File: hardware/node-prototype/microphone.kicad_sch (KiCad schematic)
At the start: 1 part, among them U2 MAX9814

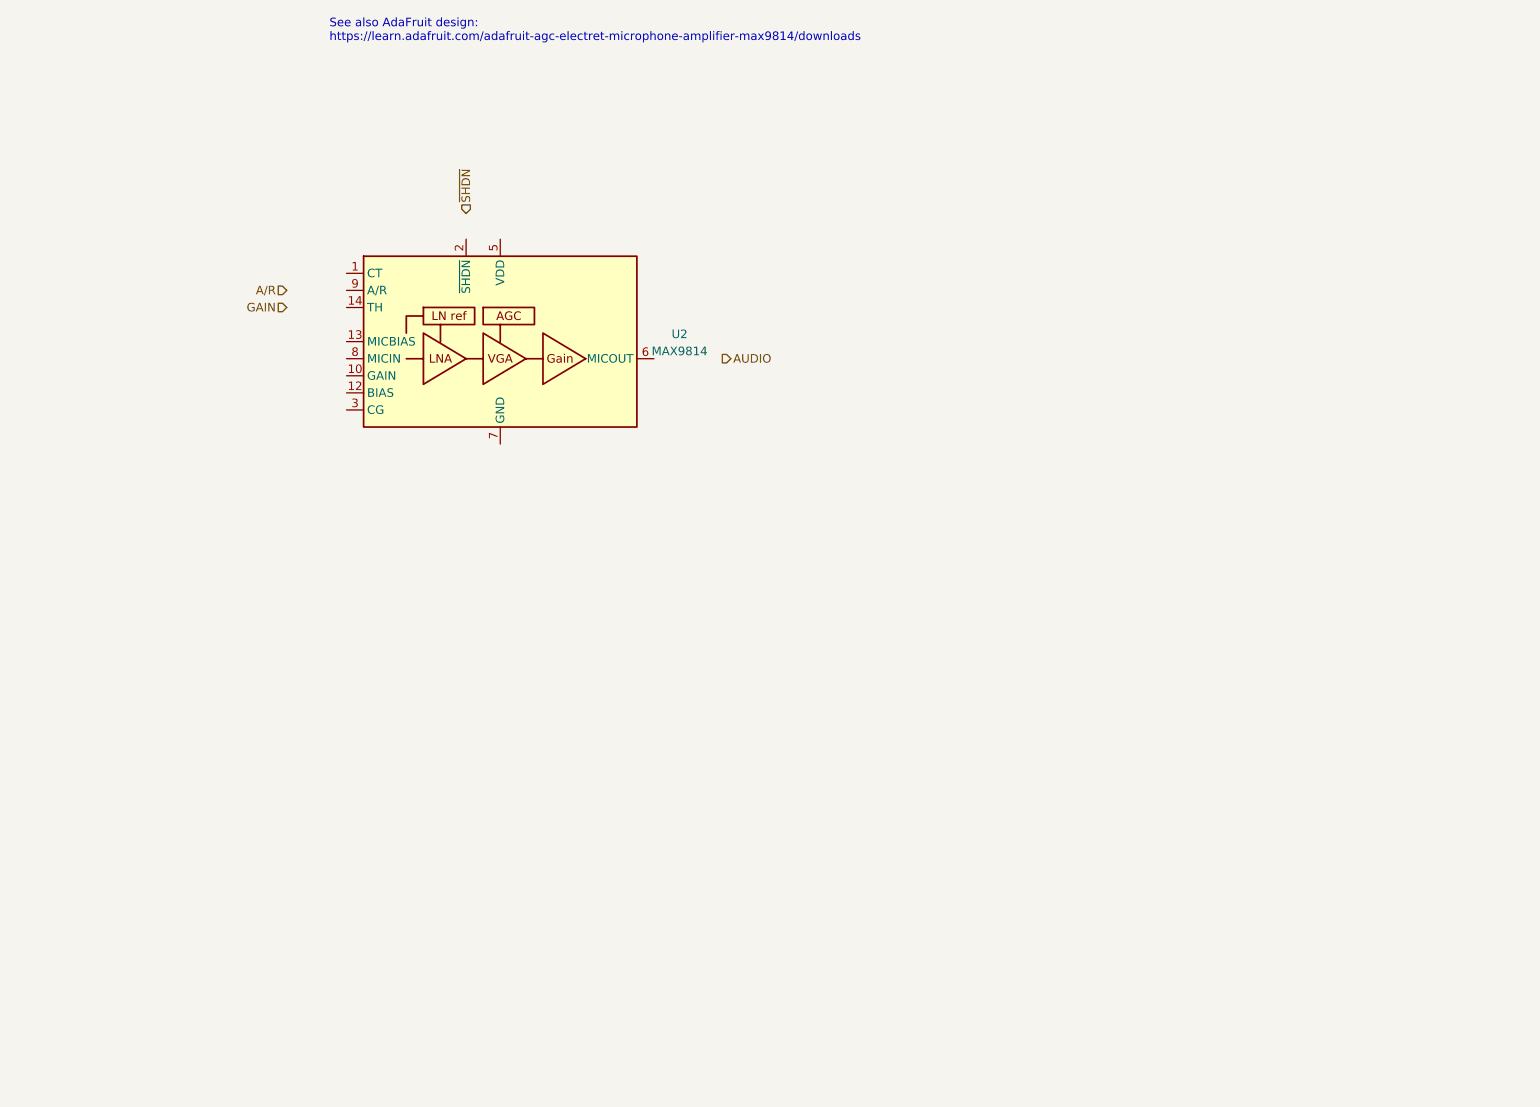
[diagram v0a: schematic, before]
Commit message: Design microphone component
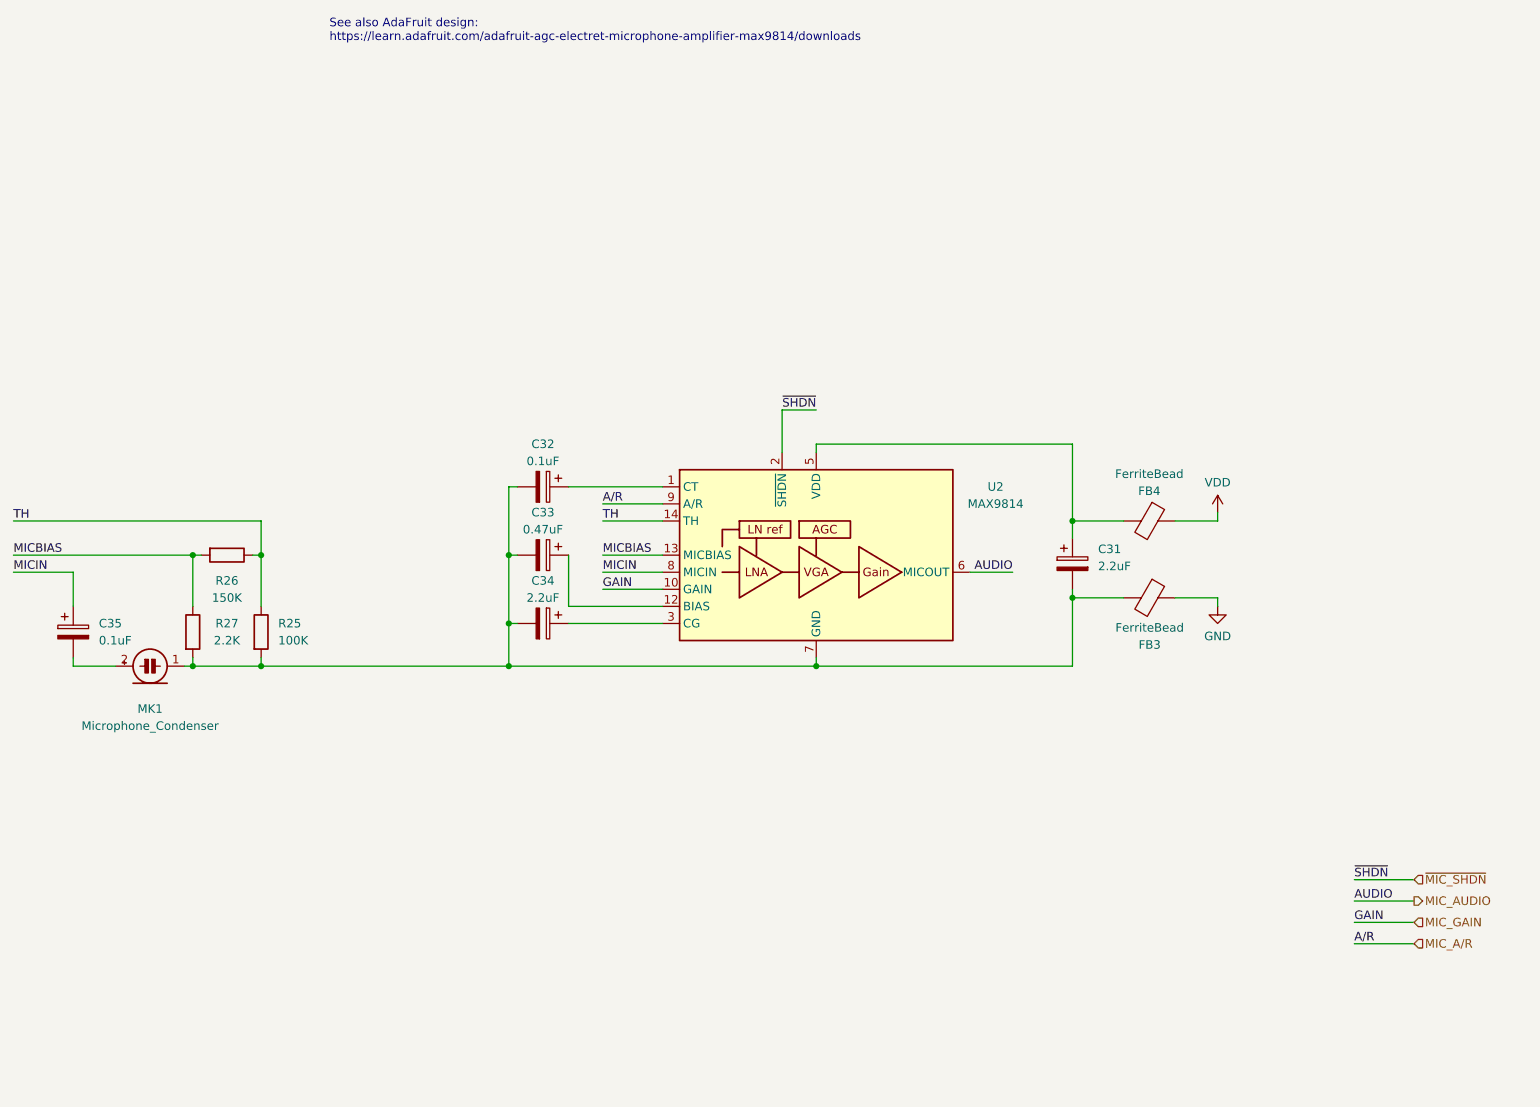
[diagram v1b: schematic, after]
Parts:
- added C31, C34: 2.2uF, symbol Device:C_Polarized
- added C32, C35: 0.1uF, symbol Device:C_Polarized
- added C33: 0.47uF, symbol Device:C_Polarized
- added FB3, FB4: FerriteBead, symbol Device:FerriteBead
- added MK1: Microphone_Condenser, symbol Device:Microphone_Condenser
- added R25: 100K, symbol Device:R
- added R26: 150K, symbol Device:R
- added R27: 2.2K, symbol Device:R
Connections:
- net at U2.1 (CT): now also C32.1
- net MIC_GAIN: now reaches U2.10 (GAIN)
- net at U2.11 (GND), U2.15 (GND), U2.4 (GND)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: now also C31.2, C32.2, C33.2, C34.2, FB3.2, MK1.1 (-), R25.2, R27.2
- net at U2.12 (BIAS): now also C33.1
- net MICBIAS: now reaches U2.13 (MICBIAS)
- net MICBIAS: now also R26.2, R27.1
- net TH: now reaches U2.14 (TH)
- net TH: now also R25.1, R26.1
- net ~{MIC_SHDN}: now reaches U2.2 (~{SHDN})
- net at U2.3 (CG): now also C34.1
- net at U2.5 (VDD): now also C31.1, FB4.2
- net MIC_AUDIO: now reaches U2.6 (MICOUT)
- net MICIN: now reaches U2.8 (MICIN)
- net MICIN: now also C35.1
- net MIC_A/R: now reaches U2.9 (A/R)
- new net: C35.2, MK1.2 (+)
- new net GND: FB3.1
- new net VDD: FB4.1
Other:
- moved on the sheet: U2

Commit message: WIP on user interface
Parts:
- removed FB3, FB4: FerriteBead, symbol Device:FerriteBead
- added R41: 10k, symbol Device:R
- R30: renamed from R27; value 2.2K -> 2.2k
- R31: renamed from R26; value 150K -> 150k
- R32: renamed from R25; value 100K -> 100k
- renumbered C35 to C31, C31 to C35, U2 to U10
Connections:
- net GND: now also C32.2, C33.2, C34.2, C35.2, MK1.1 (-), R30.2, R32.2, U10.11 (GND), U10.15 (GND), U10.4 (GND), U10.7 (GND), R41.2
- net ~{MIC_SHDN}: now also R41.1
- net VDDA: now reaches C35.1, U10.5 (VDD)

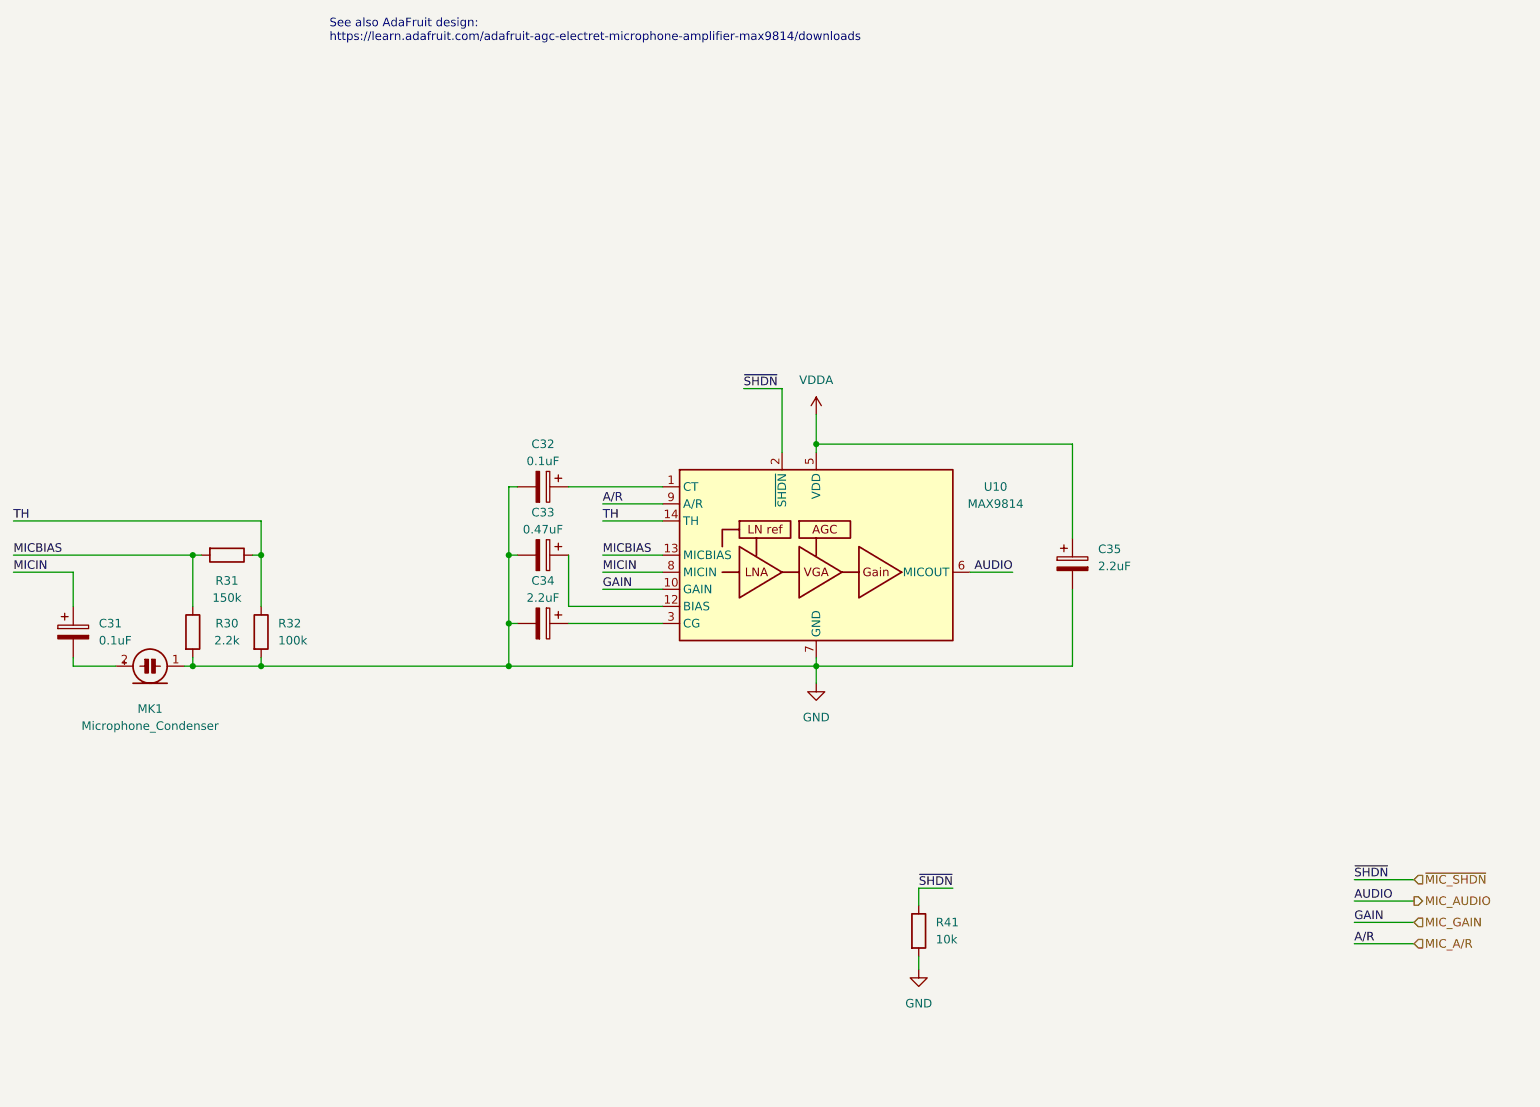
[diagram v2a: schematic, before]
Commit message: Plug schematic together
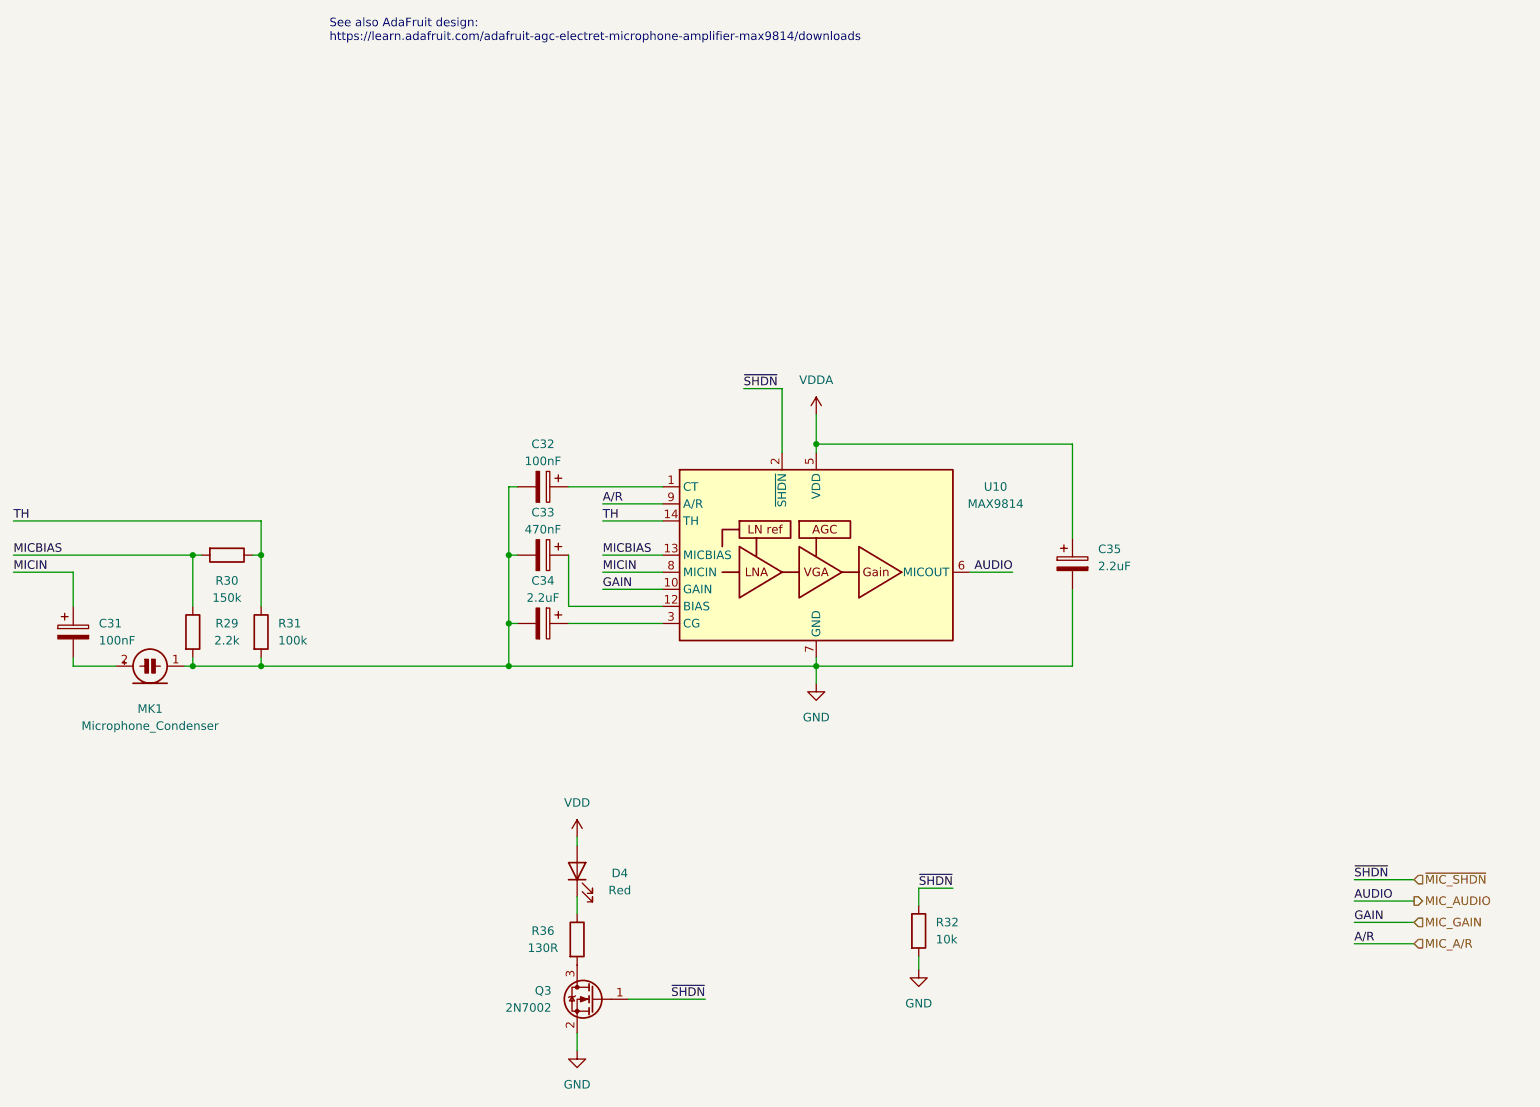
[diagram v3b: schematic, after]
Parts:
- added D4: Red, LED_SMD:LED_0603_1608Metric, symbol Device:LED
- added Q3: 2N7002, Package_TO_SOT_SMD:SOT-23, symbol Transistor_FET:2N7002
- added R36: 130R, Resistor_SMD:R_0603_1608Metric, symbol Device:R
- C31, C32: value 0.1uF -> 100nF; footprint (none) -> Capacitor_SMD:C_0603_1608Metric
- C33: value 0.47uF -> 470nF; footprint (none) -> Capacitor_SMD:C_0603_1608Metric
- C34: footprint (none) -> Capacitor_SMD:C_0603_1608Metric
- C35: footprint (none) -> LED_SMD:LED_0603_1608Metric
- MK1: footprint (none) -> MYBSP01201ABF_MYBSP00502ABF:CMA-4544PF-W
- R29: renamed from R30; footprint (none) -> Resistor_SMD:R_0603_1608Metric
- R30: renamed from R31; footprint (none) -> Resistor_SMD:R_0603_1608Metric
- R31: renamed from R32; footprint (none) -> Resistor_SMD:R_0603_1608Metric
- R32: renamed from R41; footprint (none) -> Resistor_SMD:R_0603_1608Metric
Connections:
- net GND: now also Q3.2 (S)
- net ~{MIC_SHDN}: now also Q3.1 (G)
- new net: Q3.3 (D), R36.2
- new net: D4.1 (K), R36.1
- new net VDD: D4.2 (A)

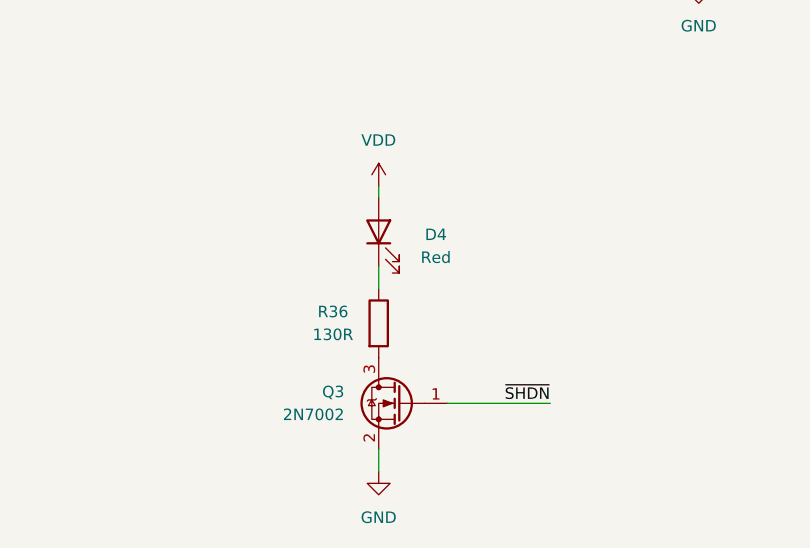
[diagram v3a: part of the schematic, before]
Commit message: Design PPS output, fix LEDs and their resistors
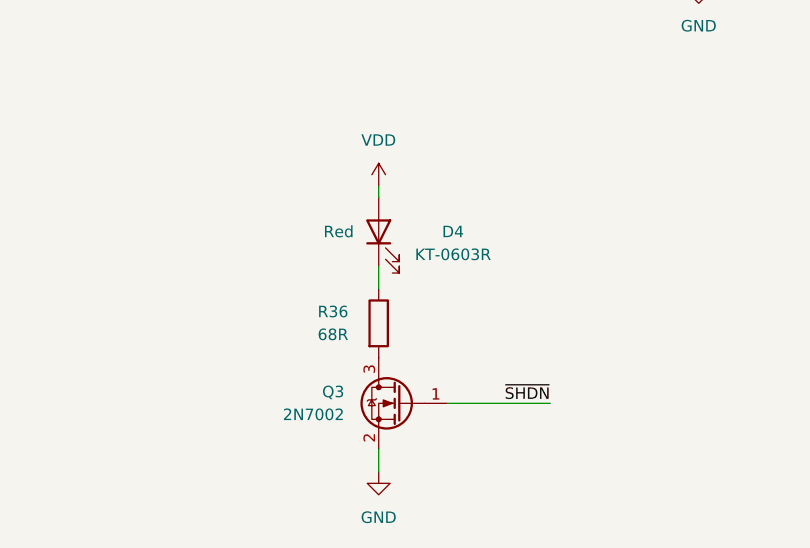
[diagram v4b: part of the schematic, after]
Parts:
- C35: footprint LED_SMD:LED_0603_1608Metric -> Capacitor_SMD:C_0603_1608Metric
- D4: value Red -> KT-0603R; Color (none) -> Red
- R36: value 130R -> 68R
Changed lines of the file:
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@@
     (instances
       (project "node-prototype"
-        (path "/294f7425-8100-4c88-a430-3b04b29ed98a/01546861-6090-4f4c-8f1c-323aafea7461"
+        (path "/294f7425-8100-4c88-a430-3b04b29ed98a/7b99f3e5-8e54-4cb2-99a1-52eeff930f06"
           (reference "Q3") (unit 1)
         )
-        (path "/294f7425-8100-4c88-a430-3b04b29ed98a/7b99f3e5-8e54-4cb2-99a1-52eeff930f06"
-          (reference "Q3") (unit 1)
-        )
       )
     )
@@
   (symbol (lib_id "Device:LED") (at 132.08 143.51 90) (unit 1)
     (in_bom yes) (on_board yes) (dnp no)
-    (property "Reference" "D4" (at 138.43 143.8275 90)
-      (effects (font (size 1.27 1.27)))
-    )
-    (property "Value" "Red" (at 138.43 146.3675 90)
+    (property "Reference" "D4" (at 140.335 143.51 90)
+      (effects (font (size 1.27 1.27)))
+    )
+    (property "Value" "KT-0603R" (at 140.335 146.05 90)
       (effects (font (size 1.27 1.27)))
     )
@@
       (effects (font (size 1.27 1.27)) hide)
     )
-    (pin "1")
-    (pin "2")
-    (instances
-      (project "node-prototype"
-        (path "/294f7425-8100-4c88-a430-3b04b29ed98a/01546861-6090-4f4c-8f1c-323aafea7461"
+    (property "Color" "Red" (at 127.635 143.51 90)
+      (effects (font (size 1.27 1.27)))
+    )
+    (pin "1")
+    (pin "2")
+    (instances
+      (project "node-prototype"
+        (path "/294f7425-8100-4c88-a430-3b04b29ed98a/7b99f3e5-8e54-4cb2-99a1-52eeff930f06"
           (reference "D4") (unit 1)
         )
-        (path "/294f7425-8100-4c88-a430-3b04b29ed98a/7b99f3e5-8e54-4cb2-99a1-52eeff930f06"
-          (reference "D4") (unit 1)
-        )
       )
     )
@@
     (instances
       (project "node-prototype"
-        (path "/294f7425-8100-4c88-a430-3b04b29ed98a/01546861-6090-4f4c-8f1c-323aafea7461"
+        (path "/294f7425-8100-4c88-a430-3b04b29ed98a/7b99f3e5-8e54-4cb2-99a1-52eeff930f06"
           (reference "#PWR055") (unit 1)
         )
-        (path "/294f7425-8100-4c88-a430-3b04b29ed98a/7b99f3e5-8e54-4cb2-99a1-52eeff930f06"
-          (reference "#PWR055") (unit 1)
-        )
       )
     )
@@
     (instances
       (project "node-prototype"
-        (path "/294f7425-8100-4c88-a430-3b04b29ed98a/01546861-6090-4f4c-8f1c-323aafea7461"
+        (path "/294f7425-8100-4c88-a430-3b04b29ed98a/7b99f3e5-8e54-4cb2-99a1-52eeff930f06"
           (reference "#PWR056") (unit 1)
         )
-        (path "/294f7425-8100-4c88-a430-3b04b29ed98a/7b99f3e5-8e54-4cb2-99a1-52eeff930f06"
-          (reference "#PWR056") (unit 1)
-        )
       )
     )
@@
       (effects (font (size 1.27 1.27)))
     )
-    (property "Value" "130R" (at 127 154.94 0)
+    (property "Value" "68R" (at 127 154.94 0)
       (effects (font (size 1.27 1.27)))
     )
@@
     (instances
       (project "node-prototype"
-        (path "/294f7425-8100-4c88-a430-3b04b29ed98a/01546861-6090-4f4c-8f1c-323aafea7461"
-          (reference "R36") (unit 1)
-        )
         (path "/294f7425-8100-4c88-a430-3b04b29ed98a/7b99f3e5-8e54-4cb2-99a1-52eeff930f06"
           (reference "R36") (unit 1)
@@
       (effects (font (size 1.27 1.27)) (justify left))
     )
-    (property "Footprint" "LED_SMD:LED_0603_1608Metric" (at 206.7052 101.6 0)
-      (effects (font (size 1.27 1.27)) hide)
-    )
+    (property "Footprint" "Capacitor_SMD:C_0603_1608Metric" (at 206.7052 101.6 0)
+      (effects (font (size 1.27 1.27)) hide)
+    )
